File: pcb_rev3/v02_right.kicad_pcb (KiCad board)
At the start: 2 copper layers, 161.1 x 140.5 mm, 72 parts, among them J1 MJ-4PP-9, SW1 SW_Push, U1 ProMicro

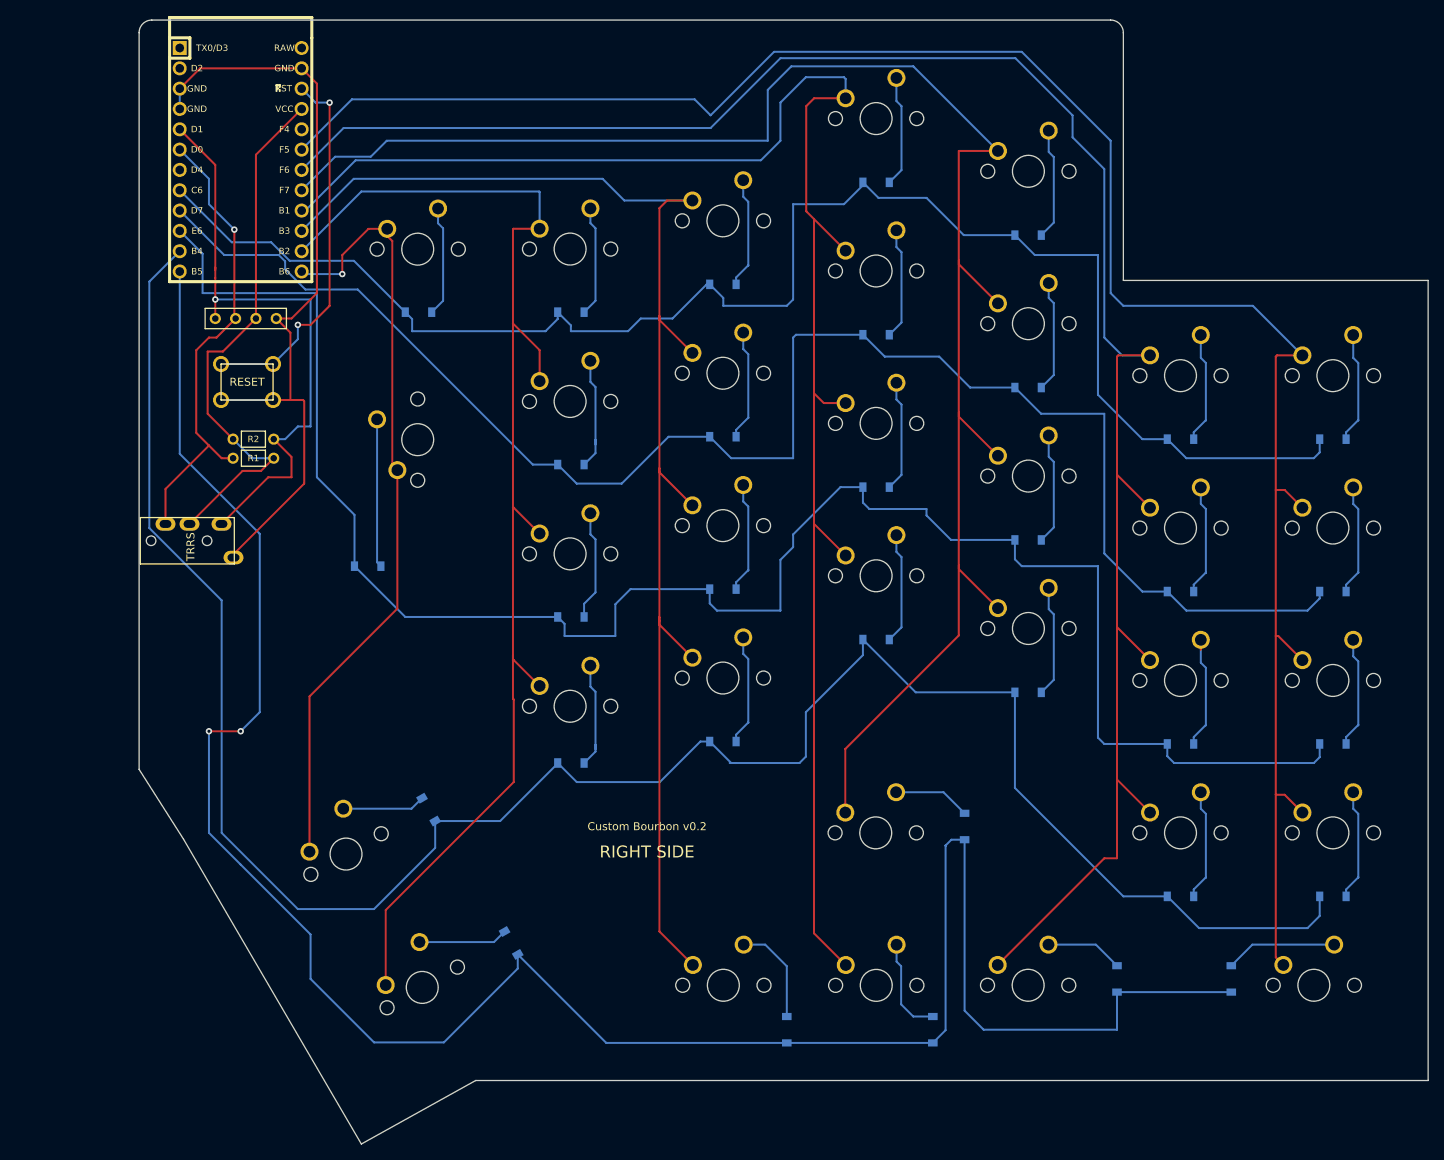
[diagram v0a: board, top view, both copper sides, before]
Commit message: Started edits for right side for v0.3; added holes for OLED cover, fixed TRRS and reset switch footprints
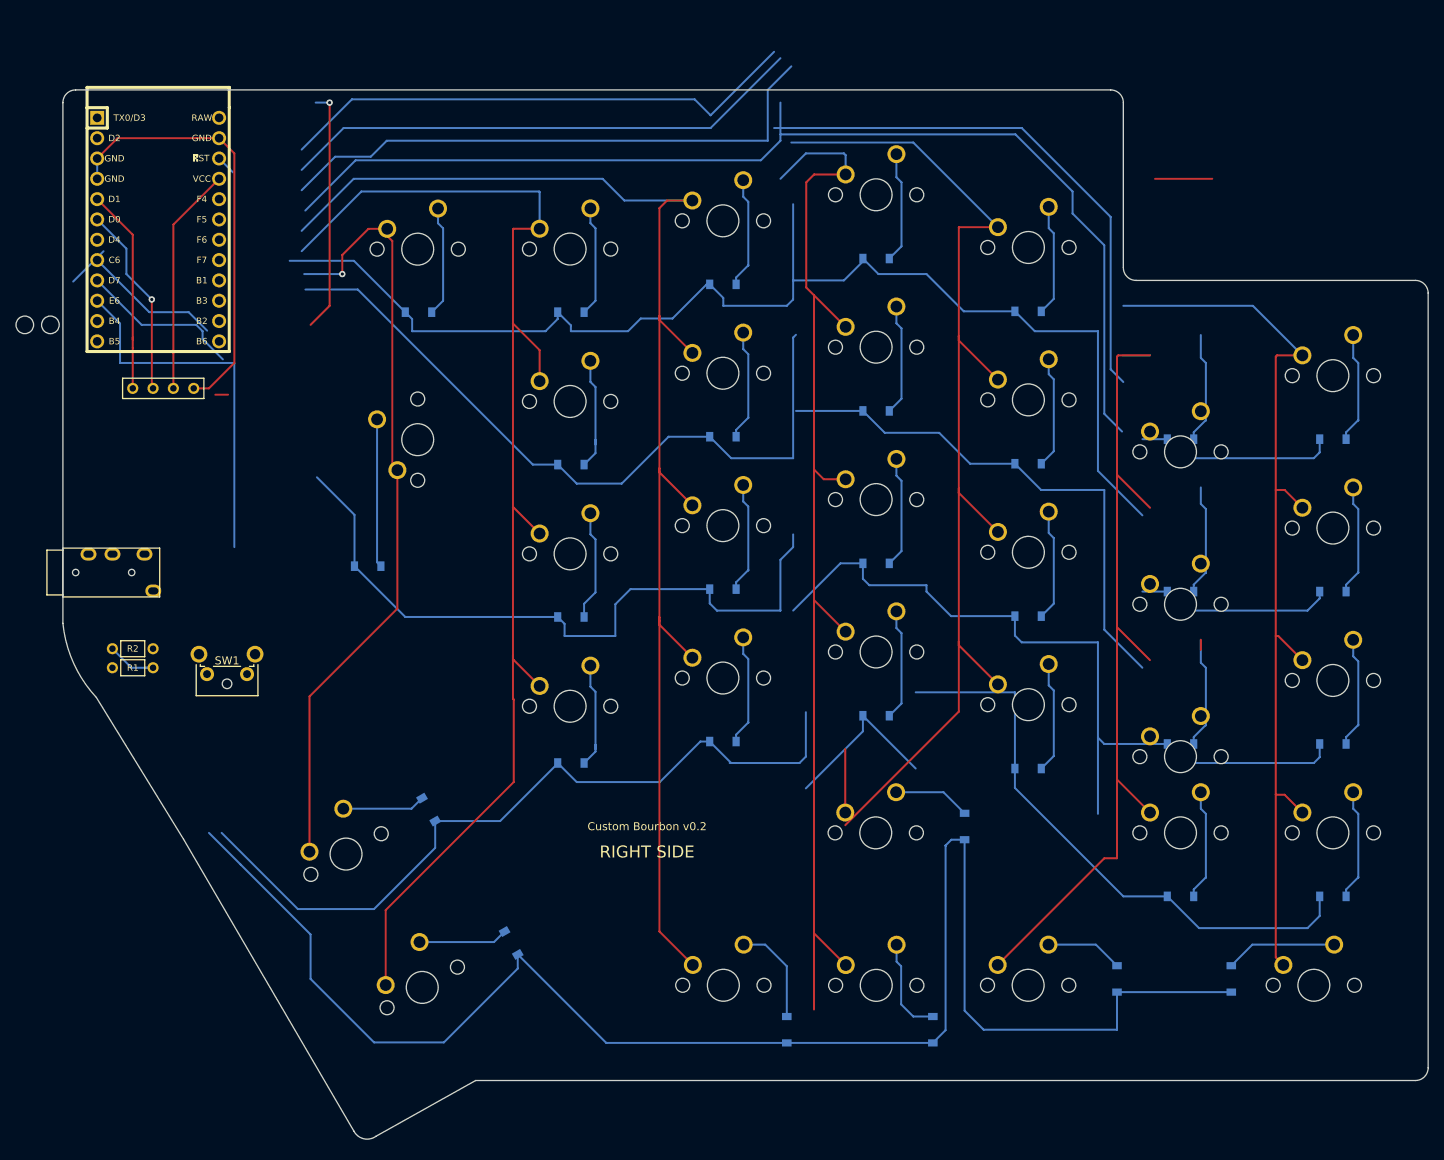
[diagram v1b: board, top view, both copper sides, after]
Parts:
- added H1: Hole, Lily58-footprint:HOLE_M2, F.Cu at (-191.3, 53.2)
- added H2: Hole, Lily58-footprint:HOLE_M2, F.Cu at (-188.1, 53.2)
- J1: value MJ-4PP-9 -> Audio-Jack-4; footprint kbd:MJ-4PP-9_1side -> Keebio-Parts:TRRS-PJ-320A
- SW1: footprint kbd:ResetSW_4P -> Keebio-Parts:SW_Tactile_SPST_Angled_MJTP1117
- moved SW1 36.5 mm to (-163.5, 96.8), turned to 180 degrees
- moved R1 30.2 mm to (-177.8, 96.0)
- moved R2 30.2 mm to (-177.8, 93.7)
- moved OL1 13.5 mm to (-177.8, 61.1)
- moved U1 13.5 mm to (-174.6, 41.3)
- moved J1 10.3 mm to (-186.5, 84.1)
- moved D12 9.53 mm to (-65.9, 70.5)
- moved D22 9.53 mm to (-65.9, 89.6)
- moved D32 9.53 mm to (-65.9, 108.6)
- moved D33 9.53 mm to (-84.9, 102.0)
- moved MX01 9.53 mm to (-46.8, 69.1)
- moved MX02 9.53 mm to (-65.8, 43.5)
- moved MX11 9.53 mm to (-46.8, 88.1)
- moved MX13 9.53 mm to (-84.9, 56.0)
- moved MX21 9.53 mm to (-46.8, 107.2)
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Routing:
- net row4: track 282.5 -> 203.3 mm, vias 2 -> 0
- net row3: track 270.3 -> 197.6 mm
- net col3: track 211.4 -> 283.4 mm
- net col1: track 247.4 -> 175.4 mm
- net SDA: track 76.2 -> 25.8 mm, vias 1 -> 0
- net GND: track 99.1 -> 54.1 mm
- net SCL: track 58.9 -> 24.0 mm
- net VCC: track 69.9 -> 35.9 mm
- net RESET: track 47.2 -> 34.6 mm, vias 2 -> 1
- net (no net): track 0.00 -> 7.14 mm
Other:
- board size 161.1 x 140.5 mm -> 170.7 x 131.2 mm

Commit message: Fixed routing for right side for v0.3
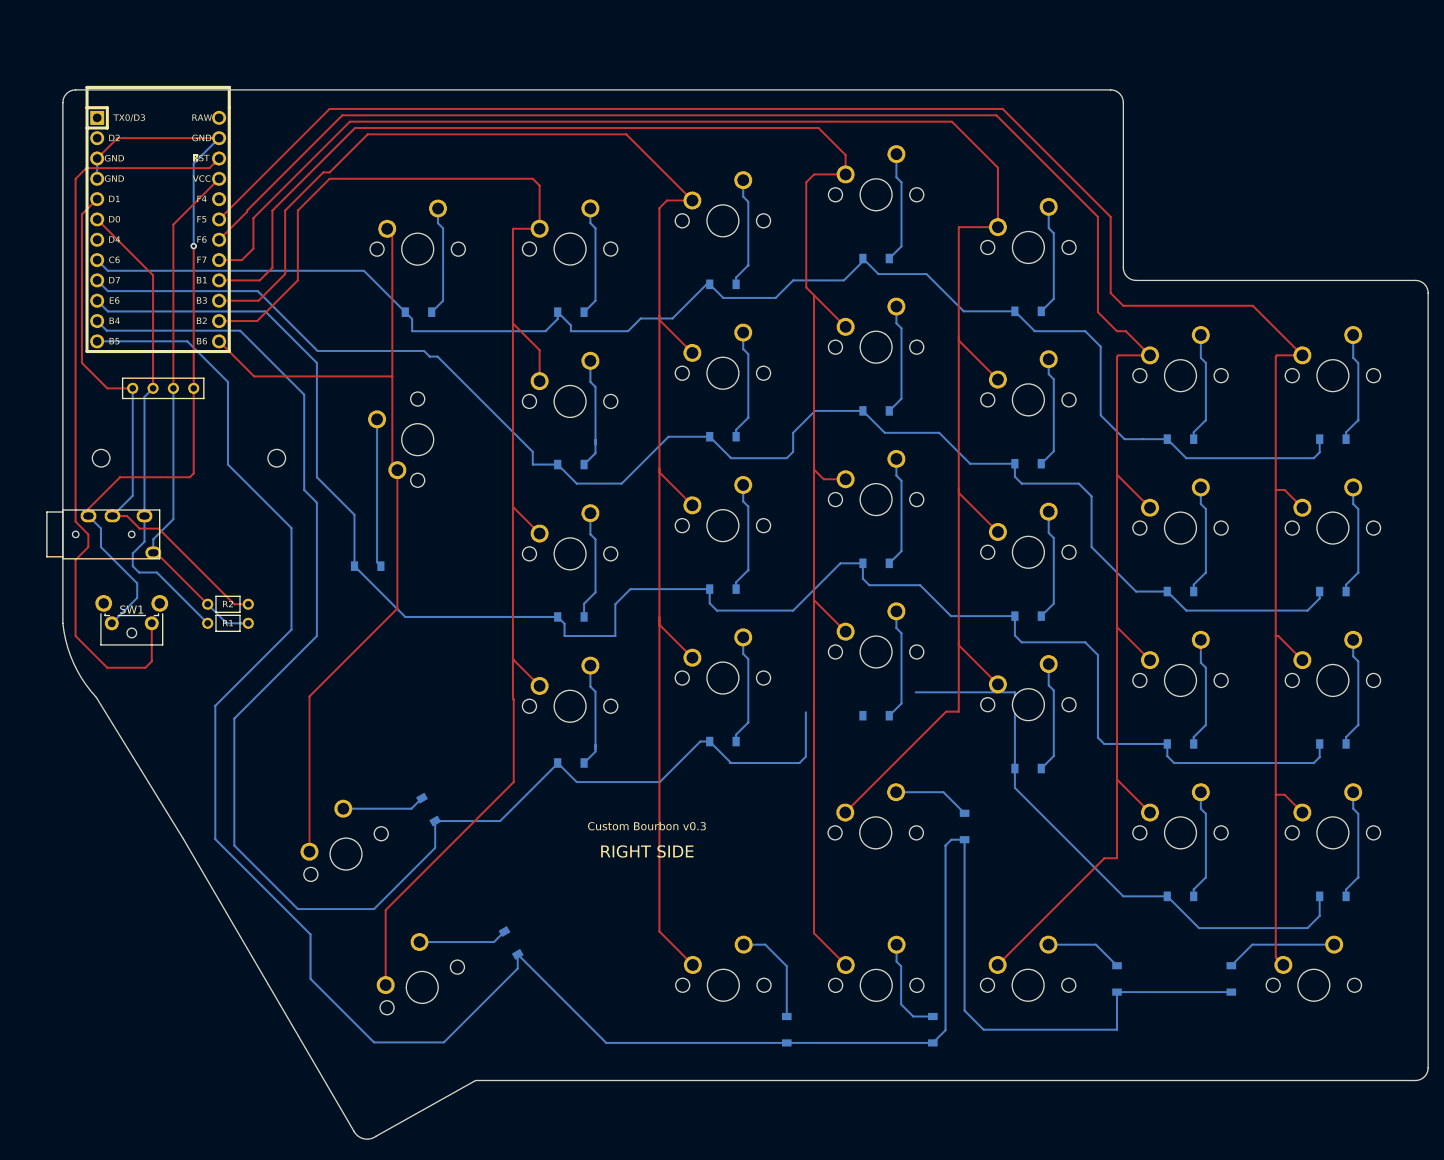
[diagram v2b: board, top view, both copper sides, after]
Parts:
- moved H2 32.8 mm to (-159.8, 69.8)
- moved H1 19.2 mm to (-181.8, 69.8)
- moved SW1 13.5 mm to (-175.4, 90.5)
- moved R1 13.1 mm to (-165.9, 90.5)
- moved R2 13.1 mm to (-165.9, 88.1)
- moved MX01 9.53 mm to (-46.8, 59.5)
- moved MX11 9.53 mm to (-46.8, 78.6)
- moved MX21 9.53 mm to (-46.8, 97.6)
- moved J1 4.76 mm to (-186.5, 79.4)
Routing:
- net row4: track 203.3 -> 285.0 mm
- net col1: track 175.4 -> 248.6 mm
- net col3: track 283.4 -> 216.3 mm
- net row3: track 197.6 -> 259.6 mm
- net RESET: track 34.6 -> 93.7 mm, vias 1 -> 0
- net SDA: track 25.8 -> 67.5 mm
- net GND: track 54.1 -> 95.2 mm, vias 0 -> 1
- net SCL: track 24.0 -> 59.8 mm, vias 1 -> 0
- net VCC: track 35.9 -> 66.7 mm
- net col4: track 172.9 -> 196.1 mm
- net col5: track 160.4 -> 181.3 mm
- net row2: track 235.4 -> 214.6 mm
- net row0: track 197.8 -> 183.0 mm
- net row1: track 202.0 -> 188.1 mm
- net col6: track 97.5 -> 107.7 mm, vias 1 -> 0
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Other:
- board text added: "Custom Bourbon v0.3"
- board text removed: "Custom Bourbon v0.2"

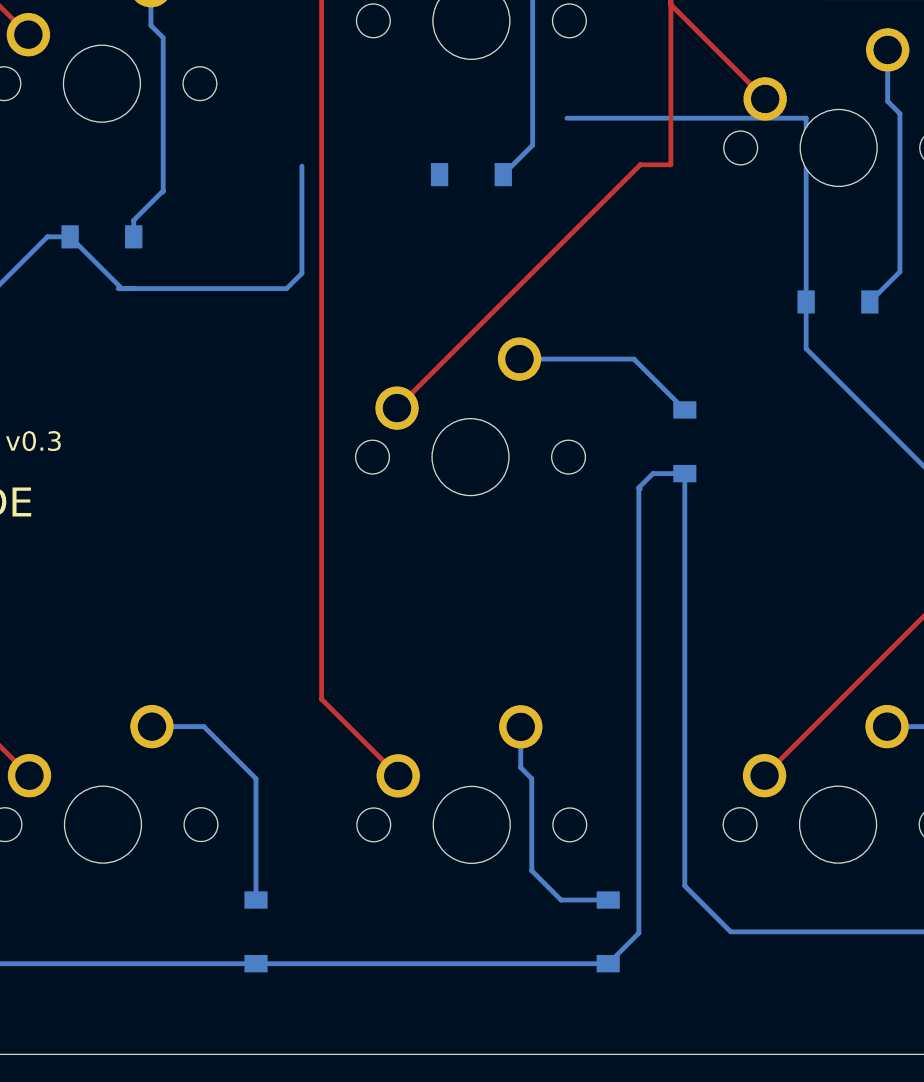
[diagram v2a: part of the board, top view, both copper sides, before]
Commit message: Finalized routing for right side of v0.3
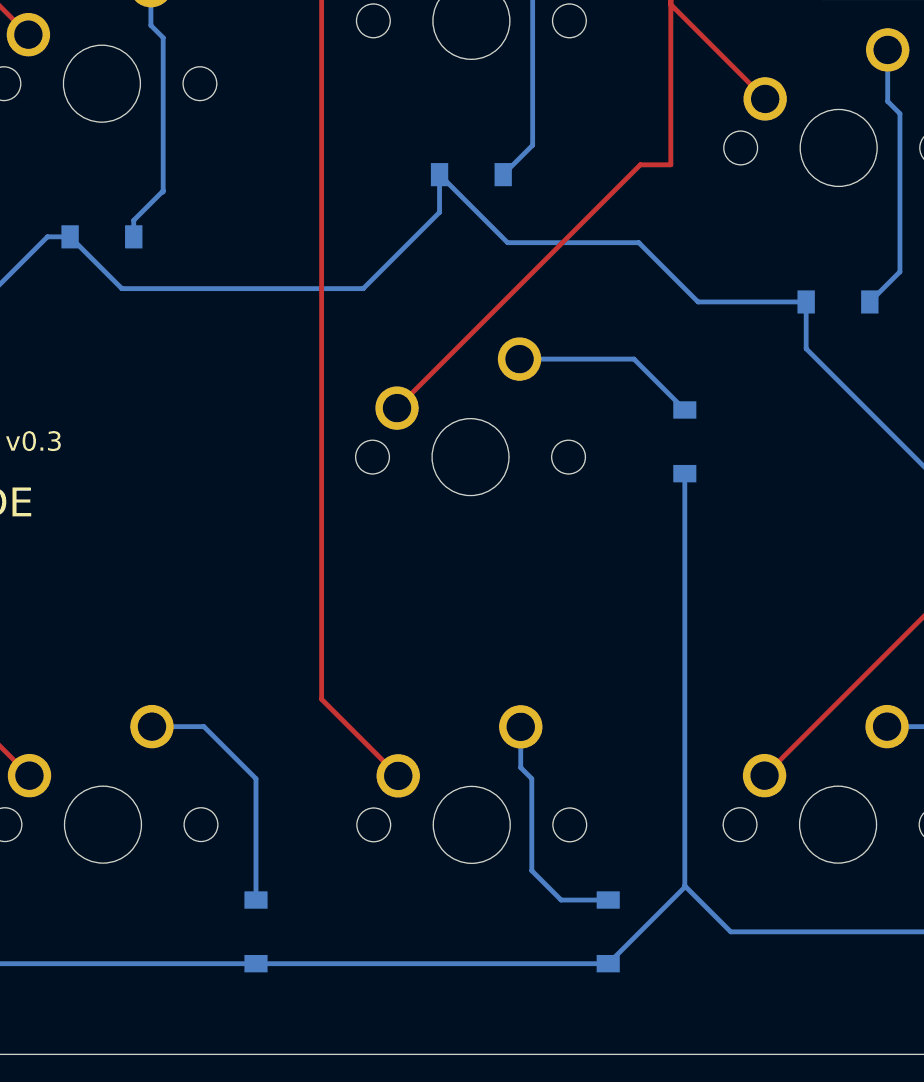
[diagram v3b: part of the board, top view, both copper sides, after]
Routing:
- net row4: track 285.0 -> 262.6 mm
- net row3: track 259.6 -> 263.5 mm
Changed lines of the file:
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@@
     (thickness 1.6)
     (drawings 25)
-    (tracks 524)
+    (tracks 522)
     (zones 0)
     (modules 74)
@@
   (segment (start -29.43125 124.61875) (end -29.43125 127.0625) (width 0.25) (layer B.Cu) (net 25))
   (segment (start -48.48125 124.61875) (end -53.975 124.61875) (width 0.25) (layer B.Cu) (net 25))
-  (segment (start -67.53 111.06375) (end -67.53 99.115) (width 0.25) (layer B.Cu) (net 25))
   (segment (start -53.975 124.61875) (end -67.53 111.06375) (width 0.25) (layer B.Cu) (net 25))
-  (segment (start -67.53 99.115) (end -79.93 99.115) (width 0.25) (layer B.Cu) (net 25))
-  (segment (start -93.6625 101.6) (end -93.6625 107.15625) (width 0.25) (layer B.Cu) (net 25))
-  (segment (start -93.6625 107.15625) (end -94.45625 107.95) (width 0.25) (layer B.Cu) (net 25))
   (segment (start -102.995 107.95) (end -105.68 105.265) (width 0.25) (layer B.Cu) (net 25))
-  (segment (start -102.39375 107.95) (end -102.995 107.95) (width 0.25) (layer B.Cu) (net 25))
-  (segment (start -94.45625 107.95) (end -102.39375 107.95) (width 0.25) (layer B.Cu) (net 25))
-  (segment (start -102.39375 107.95) (end -103.1875 107.95) (width 0.25) (layer B.Cu) (net 25))
   (segment (start -105.68 105.265) (end -106.8525 105.265) (width 0.25) (layer B.Cu) (net 25))
   (segment (start -106.8525 105.265) (end -111.91875 110.33125) (width 0.25) (layer B.Cu) (net 25))
@@
   (segment (start -139.99375 118.5625) (end -147.6375 126.20625) (width 0.25) (layer B.Cu) (net 25))
   (segment (start -139.99375 115.203942) (end -139.99375 118.5625) (width 0.25) (layer B.Cu) (net 25))
+  (segment (start -67.53 111.06375) (end -67.53 108.64) (width 0.25) (layer B.Cu) (net 25))
+  (segment (start -67.53 108.64) (end -73.12875 108.64) (width 0.25) (layer B.Cu) (net 25))
+  (segment (start -73.12875 108.64) (end -76.2 105.56875) (width 0.25) (layer B.Cu) (net 25))
+  (segment (start -83.00125 105.56875) (end -86.53 102.04) (width 0.25) (layer B.Cu) (net 25))
+  (segment (start -76.2 105.56875) (end -83.00125 105.56875) (width 0.25) (layer B.Cu) (net 25))
+  (segment (start -86.53 102.04) (end -86.53 103.9925) (width 0.25) (layer B.Cu) (net 25))
+  (segment (start -90.4875 107.95) (end -102.995 107.95) (width 0.25) (layer B.Cu) (net 25))
+  (segment (start -86.53 103.9925) (end -90.4875 107.95) (width 0.25) (layer B.Cu) (net 25))
   (segment (start -44.29125 111.60125) (end -44.29125 113.665) (width 0.25) (layer B.Cu) (net 26))
   (segment (start -44.29125 113.665) (end -43.65625 114.3) (width 0.25) (layer B.Cu) (net 26))
@@
   (segment (start -71.4375 141.2875) (end -73.81875 138.90625) (width 0.25) (layer B.Cu) (net 33))
   (segment (start -73.81875 138.90625) (end -73.81875 117.5375) (width 0.25) (layer B.Cu) (net 33))
-  (segment (start -73.81875 117.5375) (end -75.46875 117.5375) (width 0.25) (layer B.Cu) (net 33))
-  (segment (start -75.46875 117.5375) (end -76.2 118.26875) (width 0.25) (layer B.Cu) (net 33))
-  (segment (start -76.2 118.26875) (end -76.13125 118.3375) (width 0.25) (layer B.Cu) (net 33))
-  (segment (start -76.2 141.35) (end -77.7875 142.9375) (width 0.25) (layer B.Cu) (net 33))
-  (segment (start -76.2 118.26875) (end -76.2 141.35) (width 0.25) (layer B.Cu) (net 33))
   (segment (start -77.7875 142.9375) (end -96.04375 142.9375) (width 0.25) (layer B.Cu) (net 33))
   (segment (start -118.610192 142.9375) (end -129.675 131.872692) (width 0.25) (layer B.Cu) (net 33))
@@
   (segment (start -170.97375 55.245) (end -182.245 55.245) (width 0.25) (layer B.Cu) (net 33))
   (segment (start -165.89375 60.325) (end -170.97375 55.245) (width 0.25) (layer B.Cu) (net 33))
+  (segment (start -73.81875 138.96875) (end -77.7875 142.9375) (width 0.25) (layer B.Cu) (net 33))
+  (segment (start -73.81875 138.90625) (end -73.81875 138.96875) (width 0.25) (layer B.Cu) (net 33))
   (segment (start -57.405 130.65125) (end -54.76875 133.2875) (width 0.25) (layer B.Cu) (net 34))
   (segment (start -63.335 130.65125) (end -57.405 130.65125) (width 0.25) (layer B.Cu) (net 34))
